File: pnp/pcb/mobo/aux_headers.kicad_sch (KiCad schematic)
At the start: 1 part, among them J21 qwiic

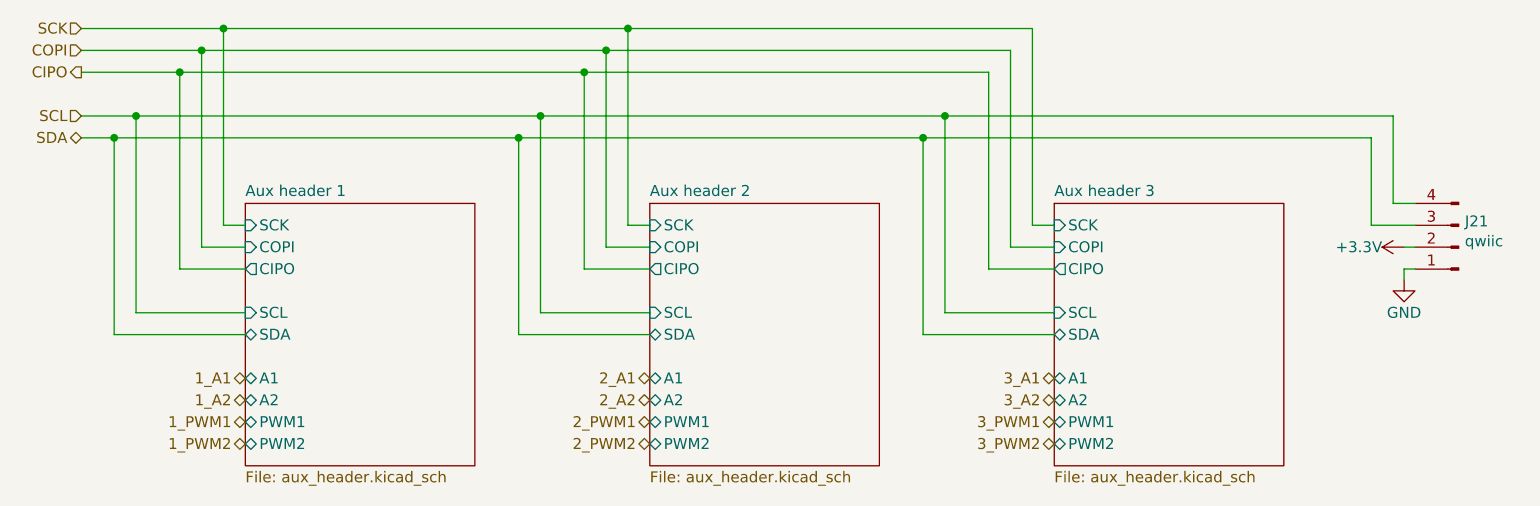
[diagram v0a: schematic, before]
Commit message: first commit of rev04 mobo beta 0. makes solder-selectable jumpers on back side of board not jumped to work with kit drivers, y2 motor port rotated correctly, moves traces out from underneath solder jumpers, adds 0 ohm jumpers to bypass the usb hub, adds 4 pin DIN connector for power, adds large decoupling cap on power supply input to decrease rippling, changes diode choice for 5v multiplexer to one already in the BOM, flips resistors on mos1 to be less confusing
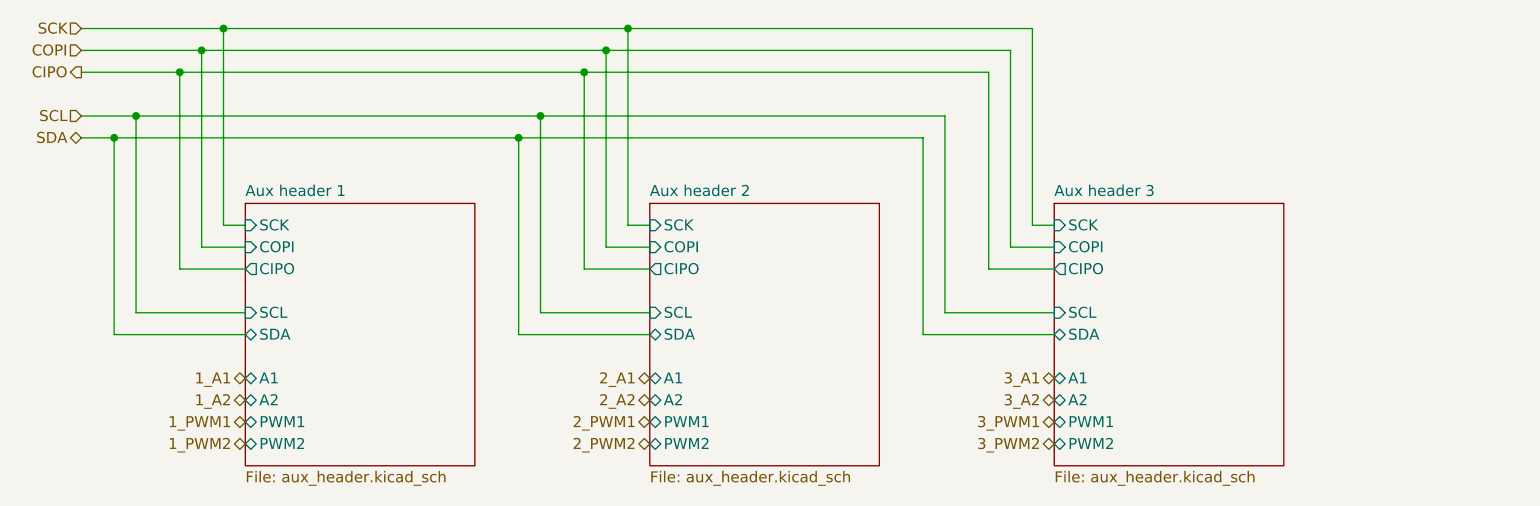
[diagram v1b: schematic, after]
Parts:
- removed J21: qwiic, Connector_JST:JST_SH_BM04B-SRSS-TB_1x04-1MP_P1.00mm_Vertical, symbol Connector:Conn_01x04_Male
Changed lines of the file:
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@@
     (rev "003")
   )
-  (junction (at 171.45 81.28) (diameter 0) (color 0 0 0 0)
-  )
   (junction (at 85.09 73.66) (diameter 0) (color 0 0 0 0)
   )
@@
   (junction (at 90.17 68.58) (diameter 0) (color 0 0 0 0)
   )
-  (junction (at 173.99 78.74) (diameter 0) (color 0 0 0 0)
-  )
   (wire (pts (xy 90.17 91.44) (xy 90.17 68.58))
     (stroke (width 0) (type default) (color 0 0 0 0))
@@
     (stroke (width 0) (type default) (color 0 0 0 0))
   )
-  (wire (pts (xy 227.33 97.79) (xy 227.33 96.52))
-    (stroke (width 0) (type default) (color 0 0 0 0))
-  )
   (wire (pts (xy 90.17 91.44) (xy 92.71 91.44))
     (stroke (width 0) (type default) (color 0 0 0 0))
@@
     (stroke (width 0) (type default) (color 0 0 0 0))
   )
-  (wire (pts (xy 226.06 88.9) (xy 226.06 78.74))
-    (stroke (width 0) (type default) (color 0 0 0 0))
-  )
   (wire (pts (xy 137.16 91.44) (xy 137.16 68.58))
     (stroke (width 0) (type default) (color 0 0 0 0))
@@
     (stroke (width 0) (type default) (color 0 0 0 0))
   )
-  (wire (pts (xy 228.6 88.9) (xy 226.06 88.9))
-    (stroke (width 0) (type default) (color 0 0 0 0))
-  )
-  (wire (pts (xy 173.99 78.74) (xy 226.06 78.74))
-    (stroke (width 0) (type default) (color 0 0 0 0))
-  )
   (wire (pts (xy 184.15 91.44) (xy 184.15 68.58))
     (stroke (width 0) (type default) (color 0 0 0 0))
@@
     (stroke (width 0) (type default) (color 0 0 0 0))
   )
-  (wire (pts (xy 171.45 81.28) (xy 223.52 81.28))
-    (stroke (width 0) (type default) (color 0 0 0 0))
-  )
   (wire (pts (xy 132.08 96.52) (xy 132.08 73.66))
     (stroke (width 0) (type default) (color 0 0 0 0))
@@
     (stroke (width 0) (type default) (color 0 0 0 0))
   )
-  (wire (pts (xy 227.33 93.98) (xy 228.6 93.98))
-    (stroke (width 0) (type default) (color 0 0 0 0))
-  )
   (wire (pts (xy 90.17 68.58) (xy 137.16 68.58))
     (stroke (width 0) (type default) (color 0 0 0 0))
@@
     (stroke (width 0) (type default) (color 0 0 0 0))
   )
-  (wire (pts (xy 227.33 96.52) (xy 228.6 96.52))
-    (stroke (width 0) (type default) (color 0 0 0 0))
-  )
-  (wire (pts (xy 223.52 91.44) (xy 228.6 91.44))
-    (stroke (width 0) (type default) (color 0 0 0 0))
-  )
   (wire (pts (xy 127 101.6) (xy 127 78.74))
     (stroke (width 0) (type default) (color 0 0 0 0))
@@
     (stroke (width 0) (type default) (color 0 0 0 0))
   )
-  (wire (pts (xy 223.52 81.28) (xy 223.52 91.44))
-    (stroke (width 0) (type default) (color 0 0 0 0))
-  )
   (wire (pts (xy 134.62 93.98) (xy 134.62 71.12))
     (stroke (width 0) (type default) (color 0 0 0 0))
@@
     (effects (font (size 1.27 1.27)) (justify right))
   )
-  (symbol (lib_id "Connector:Conn_01x04_Male") (at 233.68 93.98 180) (unit 1)
-    (in_bom yes) (on_board yes)
-    (property "Reference" "J21" (id 0) (at 234.3912 90.9828 0)
-      (effects (font (size 1.27 1.27)) (justify right))
-    )
-    (property "Value" "qwiic" (id 1) (at 234.3912 93.2942 0)
-      (effects (font (size 1.27 1.27)) (justify right))
-    )
-    (property "Footprint" "Connector_JST:JST_SH_BM04B-SRSS-TB_1x04-1MP_P1.00mm_Vertical" (id 2) (at 233.68 93.98 0)
-      (effects (font (size 1.27 1.27)) hide)
-    )
-    (property "Datasheet" "" (id 3) (at 233.68 93.98 0)
-      (effects (font (size 1.27 1.27)) hide)
-    )
-    (property "LCSC" "C145961" (id 4) (at 233.68 93.98 0)
-      (effects (font (size 1.27 1.27)) hide)
-    )
-    (property "Config" "+qwiic" (id 5) (at 233.68 93.98 0)
-      (effects (font (size 1.27 1.27)) hide)
-    )
-    (pin "1")
-    (pin "2")
-    (pin "3")
-    (pin "4")
-  )
-  (symbol (lib_id "power:GND") (at 227.33 97.79 0) (unit 1)
-    (in_bom yes) (on_board yes)
-    (property "Reference" "#PWR0185" (id 0) (at 227.33 104.14 0)
-      (effects (font (size 1.27 1.27)) hide)
-    )
-    (property "Value" "GND" (id 1) (at 227.33 101.6 0))
-    (property "Footprint" "" (id 2) (at 227.33 97.79 0)
-      (effects (font (size 1.27 1.27)) hide)
-    )
-    (property "Datasheet" "" (id 3) (at 227.33 97.79 0)
-      (effects (font (size 1.27 1.27)) hide)
-    )
-    (pin "1")
-  )
-  (symbol (lib_id "power:+3.3V") (at 227.33 93.98 90) (unit 1)
-    (in_bom yes) (on_board yes)
-    (property "Reference" "#PWR0186" (id 0) (at 231.14 93.98 0)
-      (effects (font (size 1.27 1.27)) hide)
-    )
-    (property "Value" "+3.3V" (id 1) (at 224.79 93.98 90)
-      (effects (font (size 1.27 1.27)) (justify left))
-    )
-    (property "Footprint" "" (id 2) (at 227.33 93.98 0)
-      (effects (font (size 1.27 1.27)) hide)
-    )
-    (property "Datasheet" "" (id 3) (at 227.33 93.98 0)
-      (effects (font (size 1.27 1.27)) hide)
-    )
-    (pin "1")
-  )
   (sheet (at 92.71 88.9) (size 26.67 30.48) (fields_autoplaced)
